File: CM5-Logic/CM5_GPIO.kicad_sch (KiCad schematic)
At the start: 19 parts, among them J13 JST_SHBM04B-SRSS-TB, J14 Micro_SD_Card_Det, U5 74LVC1G07SE-7, U6 TPD4EUSB30, U7 TPD4EUSB30, U8 RT9742GGJ5, U9 MagJack-A70-112-331N126

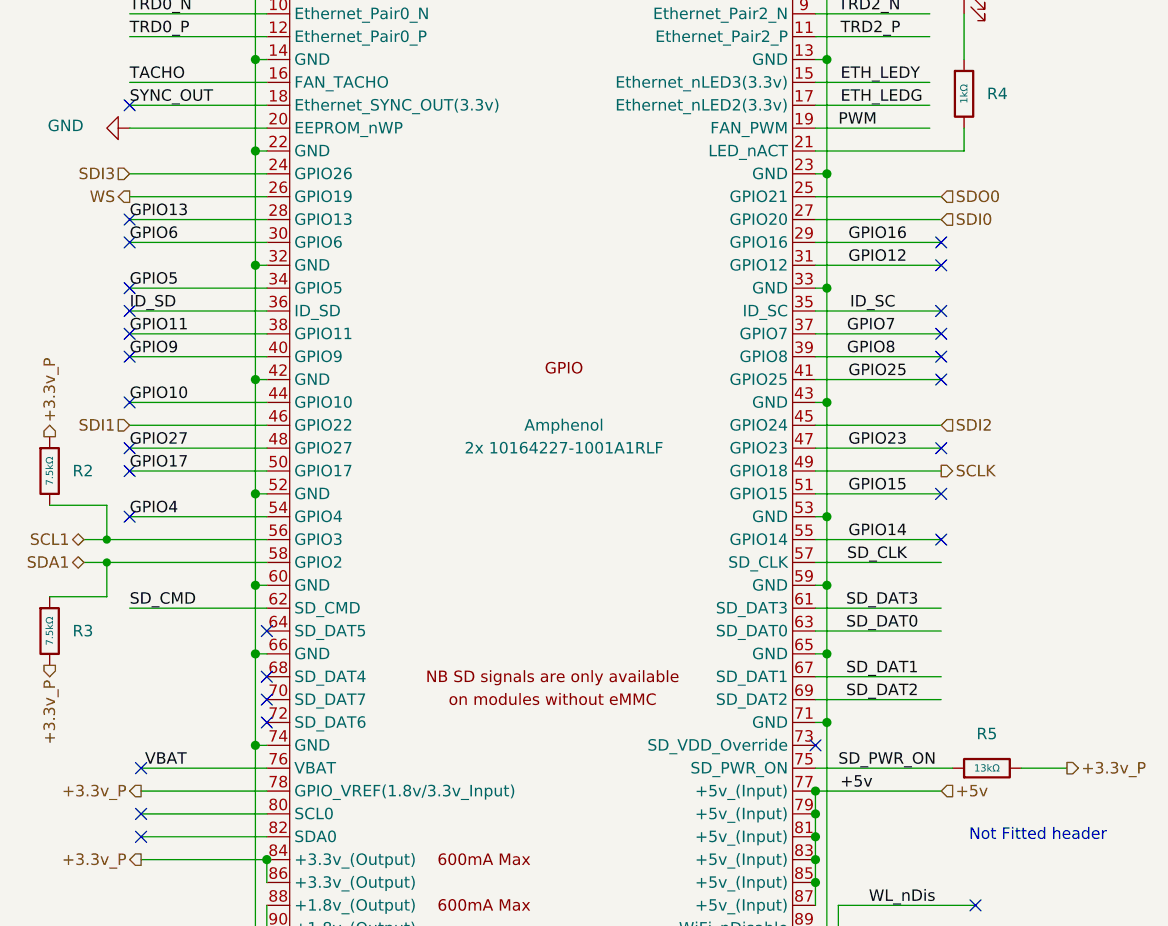
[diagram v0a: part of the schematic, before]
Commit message: adds respeaker and reworks the amplifier
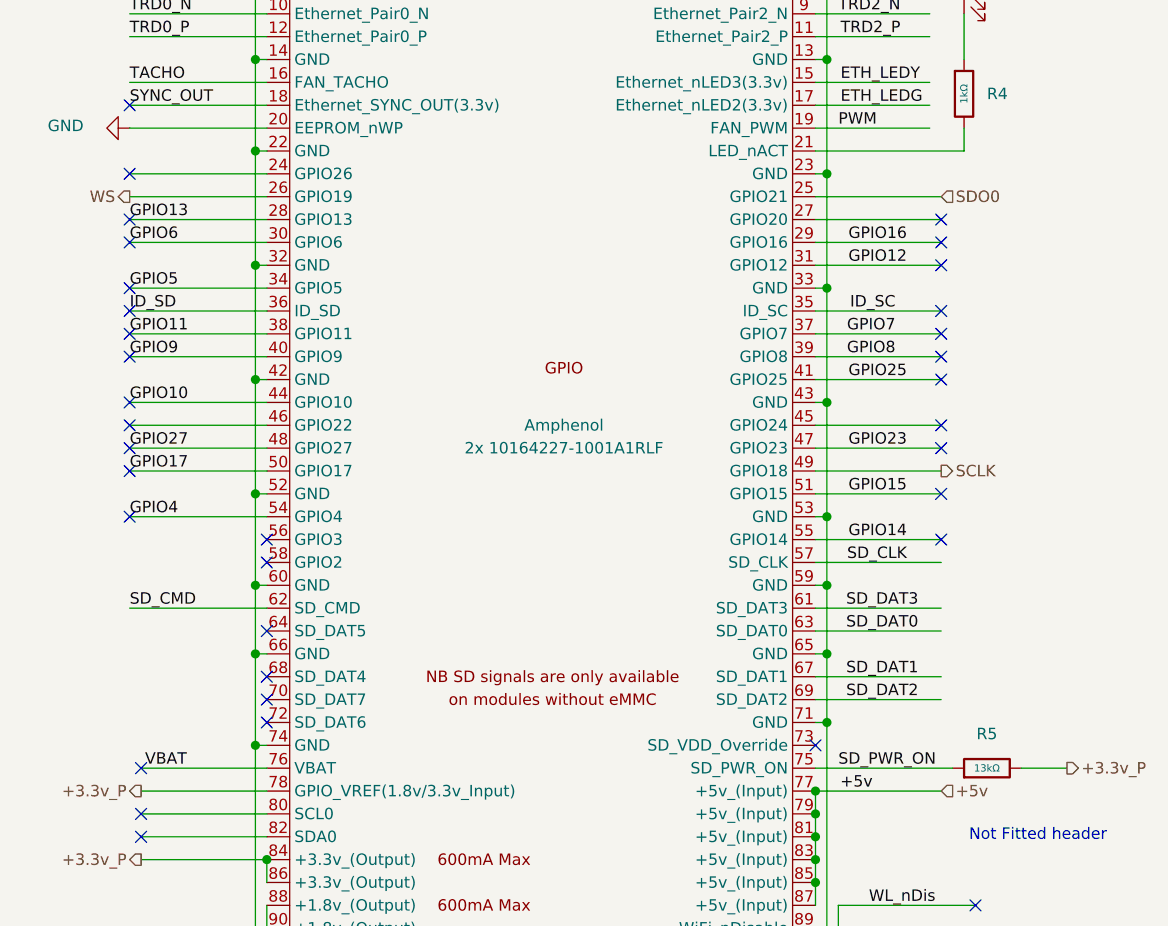
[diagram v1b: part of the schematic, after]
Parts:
- removed R2, R3: 7.5kΩ, PCM_JLCPCB:R_0402, symbol PCM_JLCPCB-Resistors:0402,7.5kΩ
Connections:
- net SCL1: no longer names the net of Module1.56 (GPIO3)
- net SDA1: no longer names the net of Module1.58 (GPIO2)
- net SDI0: no longer names the net of Module1.27 (GPIO20)
- net SDI1: no longer names the net of Module1.46 (GPIO22)
- net SDI2: no longer names the net of Module1.45 (GPIO24)
- net SDI3: no longer names the net of Module1.24 (GPIO26)
- no-connect marks 43 -> 49

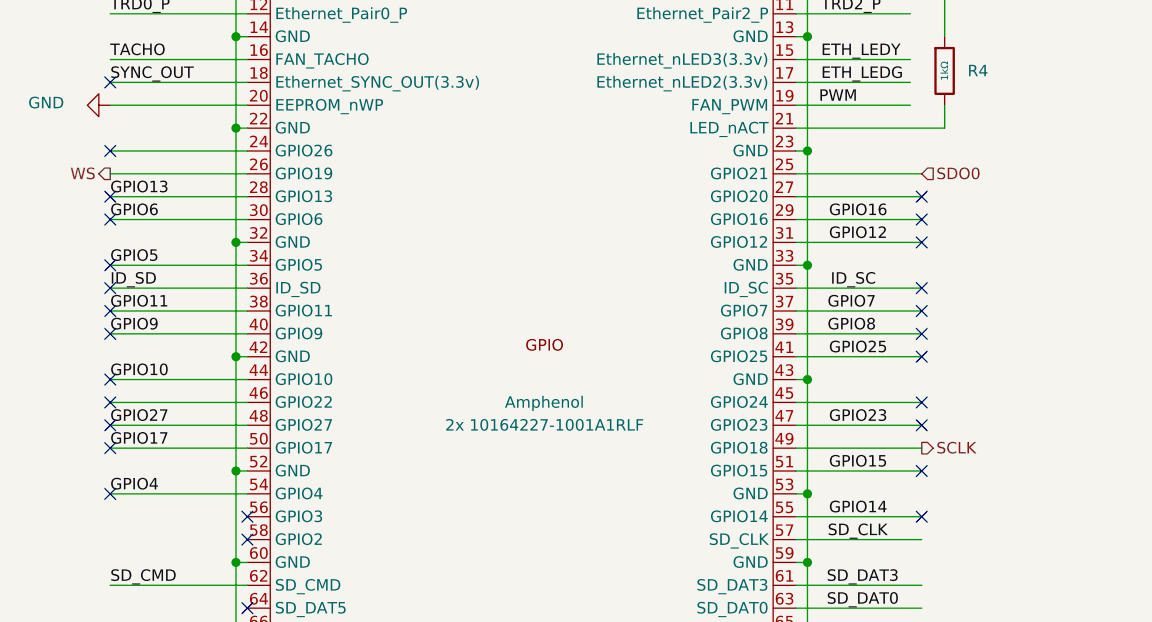
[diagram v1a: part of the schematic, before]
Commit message: fixes all label issues and power input pins
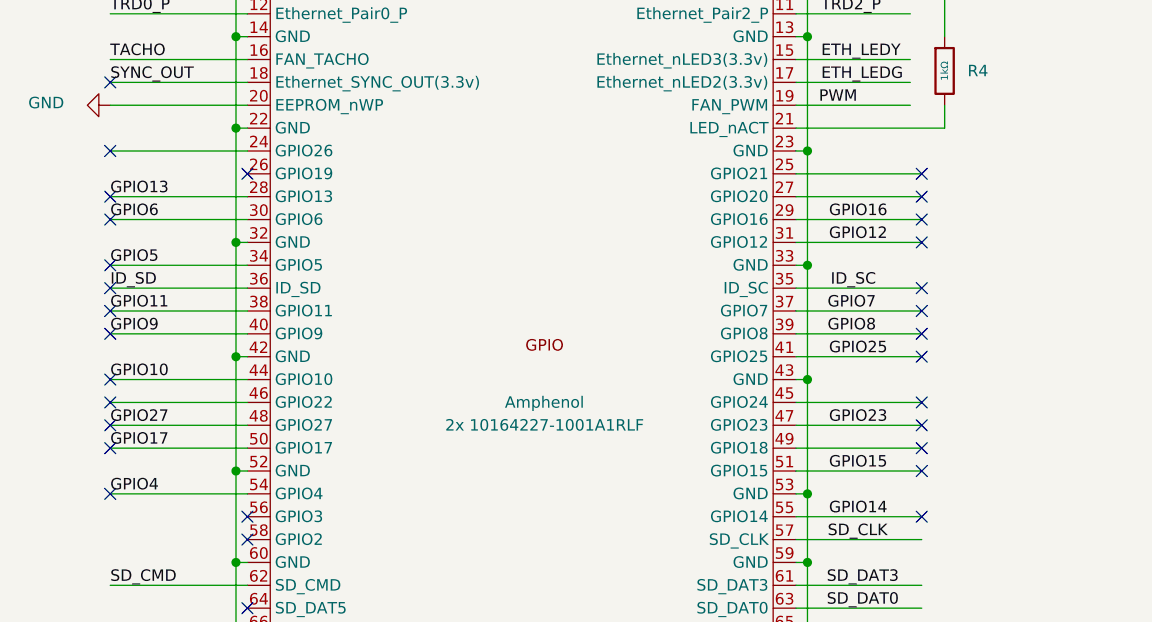
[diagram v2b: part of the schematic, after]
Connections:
- net SCLK: no longer names the net of Module1.49 (GPIO18)
- net SDO0: no longer names the net of Module1.25 (GPIO21)
- net WS: no longer names the net of Module1.26 (GPIO19)
- no-connect marks 49 -> 52
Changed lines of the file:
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@@
+	)
+	(no_connect
+		(at 134.62 53.34)
 	)
 	(no_connect
@@
 	)
 	(no_connect
+		(at 134.62 83.82)
+	)
+	(no_connect
 		(at 44.45 63.5)
 	)
@@
 	)
 	(no_connect
+		(at 59.69 53.34)
+	)
+	(no_connect
 		(at 44.45 58.42)
 	)
@@
 		(pts
 			(xy 185.42 33.02) (xy 194.31 33.02)
-		)
-		(stroke
-			(width 0)
-			(type solid)
-		)
-	)
-	(wire
-		(pts
-			(xy 44.45 53.34) (xy 59.69 53.34)
 		)
 		(stroke
@@
 		)
 	)
-	(hierarchical_label "SDO0"
-		(shape input)
-		(at 134.62 53.34 0)
-		(effects
-			(font
-				(size 1.27 1.27)
-			)
-			(justify left)
-		)
-	)
-	(hierarchical_label "WS"
-		(shape output)
-		(at 44.45 53.34 180)
-		(effects
-			(font
-				(size 1.27 1.27)
-			)
-			(justify right)
-		)
-	)
 	(hierarchical_label "+3.3v_P"
 		(shape output)
@@
 		)
 	)
-	(hierarchical_label "SCLK"
-		(shape output)
-		(at 134.62 83.82 0)
-		(effects
-			(font
-				(size 1.27 1.27)
-			)
-			(justify left)
-		)
-	)

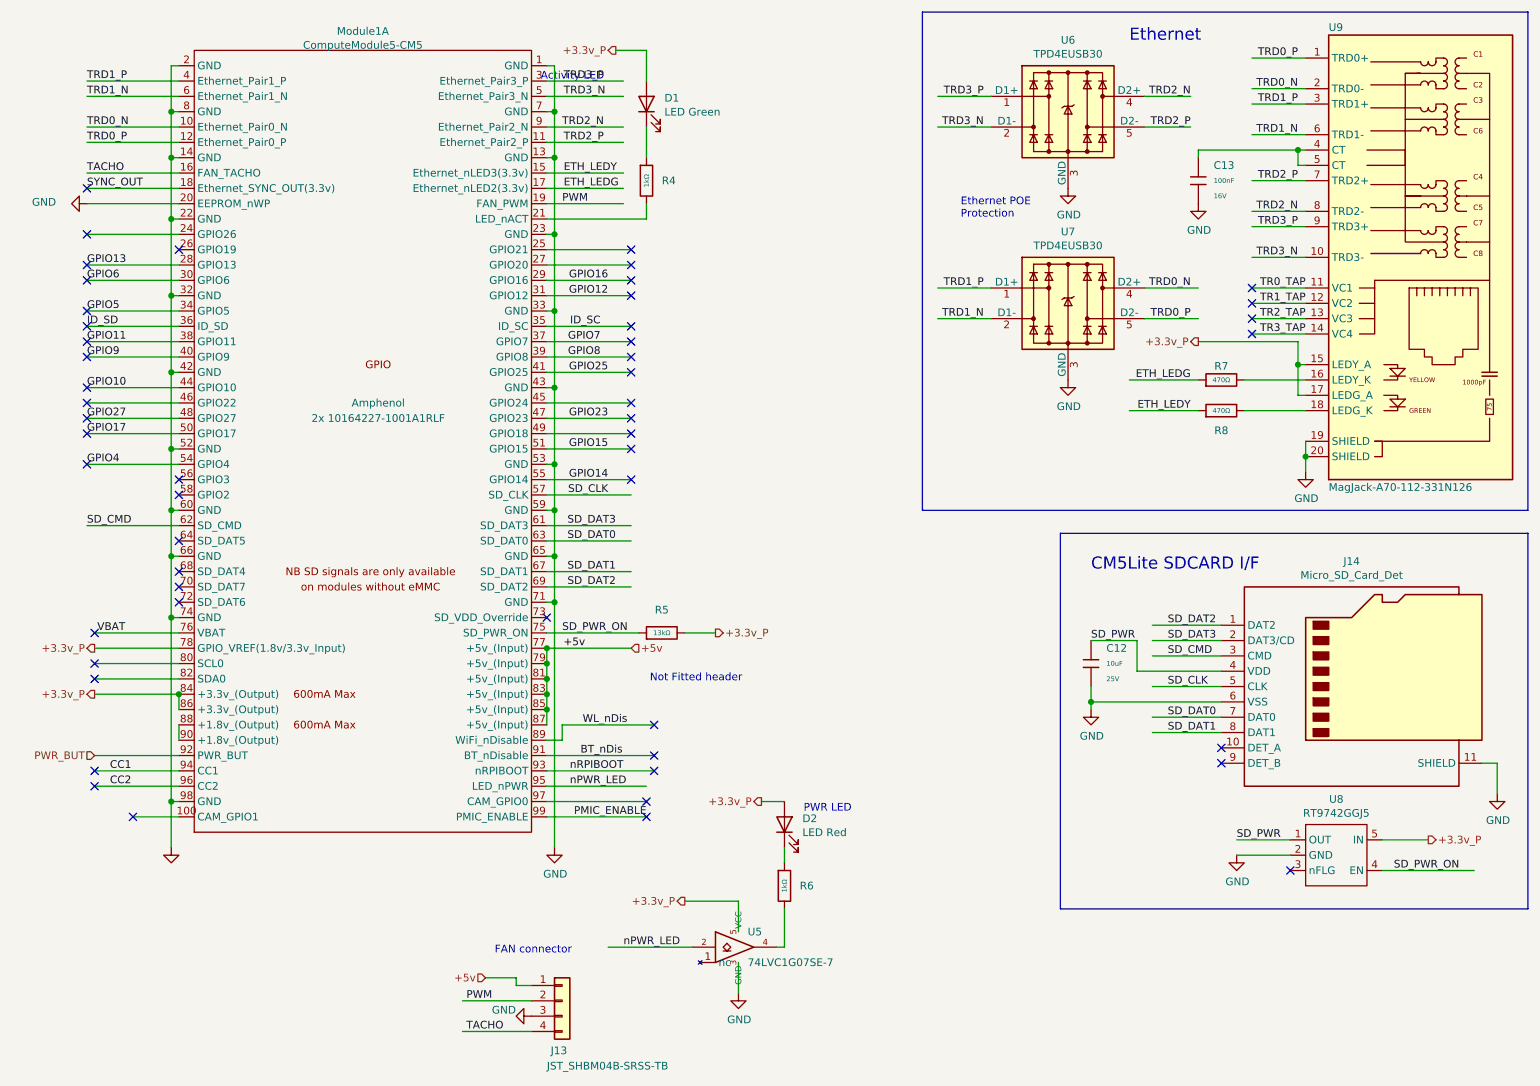
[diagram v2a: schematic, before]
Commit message: adds a 24Pin ATX PSU interface for power and cleans up the amplifier hierarchy
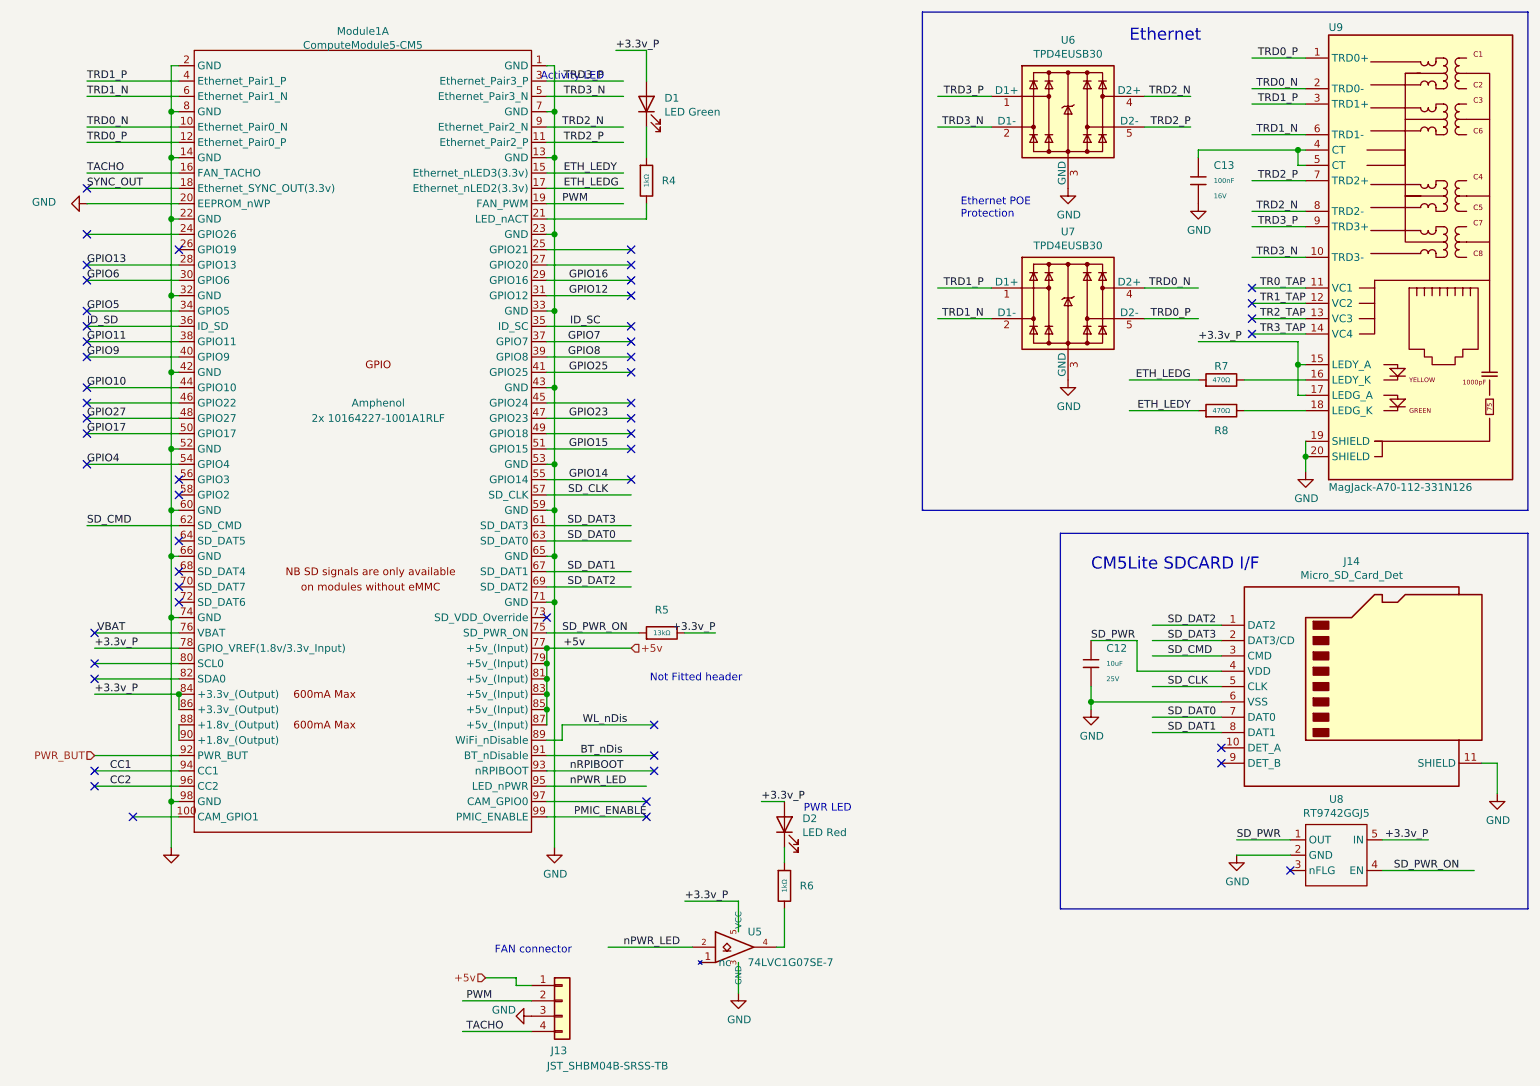
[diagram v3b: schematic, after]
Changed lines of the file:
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@@
+		)
+	)
+	(label "+3.3v_P"
+		(at 132.08 20.32 0)
+		(effects
+			(font
+				(size 1.27 1.27)
+			)
+			(justify left bottom)
 		)
 	)
@@
 		)
 	)
+	(label "+3.3v_P"
+		(at 148.59 116.84 180)
+		(effects
+			(font
+				(size 1.27 1.27)
+			)
+			(justify right bottom)
+		)
+	)
 	(label "TRD0_N"
 		(at 227.33 59.69 180)
@@
 		)
 	)
+	(label "+3.3v_P"
+		(at 143.51 161.29 0)
+		(effects
+			(font
+				(size 1.27 1.27)
+			)
+			(justify left bottom)
+		)
+	)
 	(label "SD_DAT3"
 		(at 223.52 118.11 0)
@@
 		)
 	)
+	(label "+3.3v_P"
+		(at 228.6 68.58 0)
+		(effects
+			(font
+				(size 1.27 1.27)
+			)
+			(justify left bottom)
+		)
+	)
 	(label "TRD2_N"
 		(at 123.19 33.02 0)
@@
 		)
 	)
+	(label "+3.3v_P"
+		(at 45.72 127 0)
+		(effects
+			(font
+				(size 1.27 1.27)
+			)
+			(justify left bottom)
+		)
+	)
 	(label "nRPIBOOT"
 		(at 124.46 139.7 0)
@@
 		)
 	)
+	(label "+3.3v_P"
+		(at 45.72 119.38 0)
+		(effects
+			(font
+				(size 1.27 1.27)
+			)
+			(justify left bottom)
+		)
+	)
 	(label "TRD2_N"
 		(at 245.11 46.99 180)
@@
 		)
 	)
+	(label "+3.3v_P"
+		(at 156.21 144.78 0)
+		(effects
+			(font
+				(size 1.27 1.27)
+			)
+			(justify left bottom)
+		)
+	)
 	(label "TRD1_N"
 		(at 245.11 34.29 180)
@@
 		)
 	)
+	(label "+3.3v_P"
+		(at 266.7 151.13 180)
+		(effects
+			(font
+				(size 1.27 1.27)
+			)
+			(justify right bottom)
+		)
+	)
 	(label "TR3_TAP"
 		(at 246.38 67.31 180)
@@
 			)
 			(justify right bottom)
-		)
-	)
-	(hierarchical_label "+3.3v_P"
-		(shape output)
-		(at 156.21 144.78 180)
-		(effects
-			(font
-				(size 1.27 1.27)
-			)
-			(justify right)
-		)
-	)
-	(hierarchical_label "+3.3v_P"
-		(shape output)
-		(at 228.6 68.58 180)
-		(effects
-			(font
-				(size 1.27 1.27)
-			)
-			(justify right)
 		)
 	)
@@
 		)
 	)
-	(hierarchical_label "+3.3v_P"
-		(shape output)
-		(at 148.59 116.84 0)
-		(effects
-			(font
-				(size 1.27 1.27)
-			)
-			(justify left)
-		)
-	)
 	(hierarchical_label "+5v"
 		(shape input)
@@
 		)
 	)
-	(hierarchical_label "+3.3v_P"
-		(shape output)
-		(at 45.72 119.38 180)
-		(effects
-			(font
-				(size 1.27 1.27)
-			)
-			(justify right)
-		)
-	)
 	(hierarchical_label "+5v"
 		(shape input)
@@
 		)
 	)
-	(hierarchical_label "+3.3v_P"
-		(shape output)
-		(at 45.72 127 180)
-		(effects
-			(font
-				(size 1.27 1.27)
-			)
-			(justify right)
-		)
-	)
-	(hierarchical_label "+3.3v_P"
-		(shape output)
-		(at 143.51 161.29 180)
-		(effects
-			(font
-				(size 1.27 1.27)
-			)
-			(justify right)
-		)
-	)
-	(hierarchical_label "+3.3v_P"
-		(shape output)
-		(at 266.7 151.13 0)
-		(effects
-			(font
-				(size 1.27 1.27)
-			)
-			(justify left)
-		)
-	)
-	(hierarchical_label "+3.3v_P"
-		(shape output)
-		(at 132.08 20.32 180)
-		(effects
-			(font
-				(size 1.27 1.27)
-			)
-			(justify right)
-		)
-	)
